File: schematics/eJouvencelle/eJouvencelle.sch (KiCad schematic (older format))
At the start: 28 parts

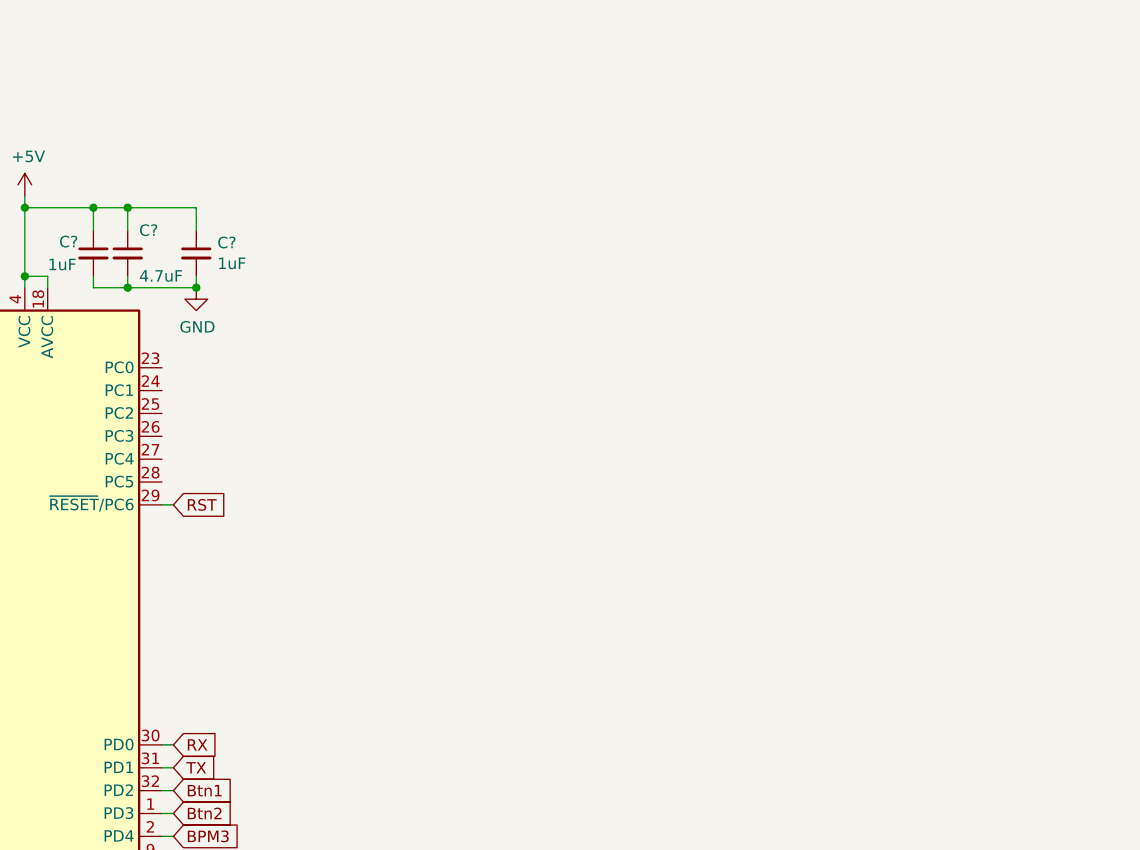
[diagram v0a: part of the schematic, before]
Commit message: add 7-segment w/ CD4511
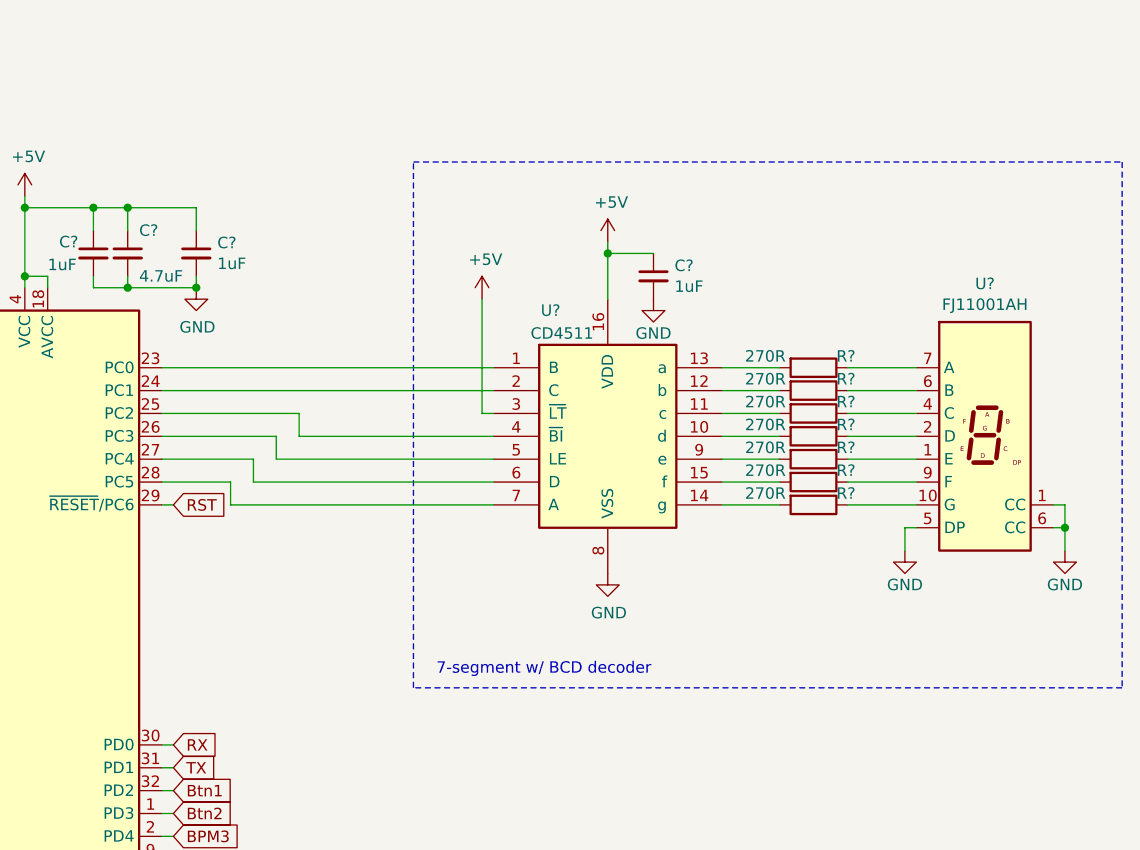
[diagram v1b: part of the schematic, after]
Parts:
- added C?: 1uF, symbol Device:C_Small
- added R? (x7): 270R, symbol Device:R
- added U?: CD4511, symbol eJouvencelle:CD4511
- added U?: FJ11001AH, Display_7Segment:HDSP-7801, symbol eJouvencelle:FJ11001AH
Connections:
- net +5V: now also C?.1, U?.16 (VDD), U?.3 (~LT)
- net GND: now also C?.2, U?.1 (E), U?.5 (DP), U?.6 (CC), U?.8 (VSS)
- net at U?.23 (PC0): now also U?.1 (B)
- net at U?.24 (PC1): now also U?.2 (C)
- net at U?.25 (PC2): now also U?.4 (~BI)
- net at U?.26 (PC3): now also U?.5 (LE)
- net at U?.27 (PC4): now also U?.6 (D)
- net at U?.28 (PC5): now also U?.7 (A)
- new net: R?.2, U?.10 (d)
- new net: R?.2, U?.11 (c)
- new net: R?.2, U?.12 (b)
- new net: R?.2, U?.13 (a)
- new net: R?.2, U?.14 (g)
- new net: R?.2, U?.15 (f)
- new net: R?.2, U?.9 (e)
- new net: R?.1, U?.7 (A)
- new net: R?.1, U?.6 (CC)
- new net: R?.1, U?.4 (C)
- new net: R?.1, U?.2 (D)
- new net: R?.1, U?.1 (E)
- new net: R?.1, U?.9 (F)
- new net: R?.1, U?.10 (G)
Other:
- note added: "7-segment w/ BCD decoder"

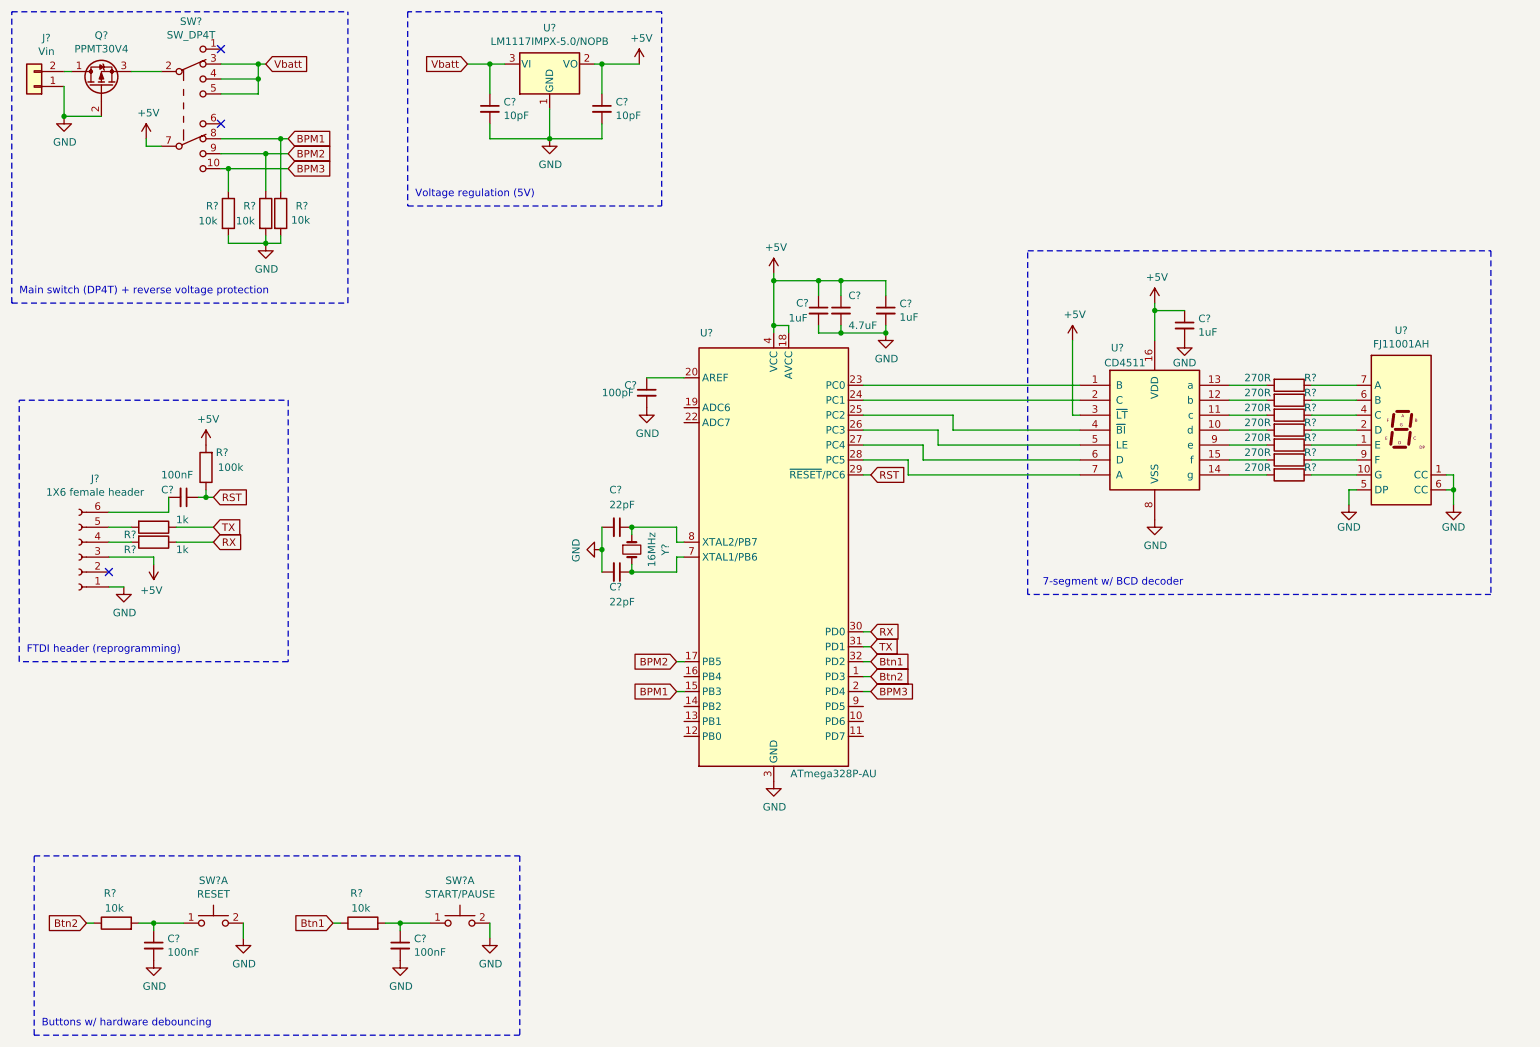
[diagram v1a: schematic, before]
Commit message: add MOSFET-driven buzzer
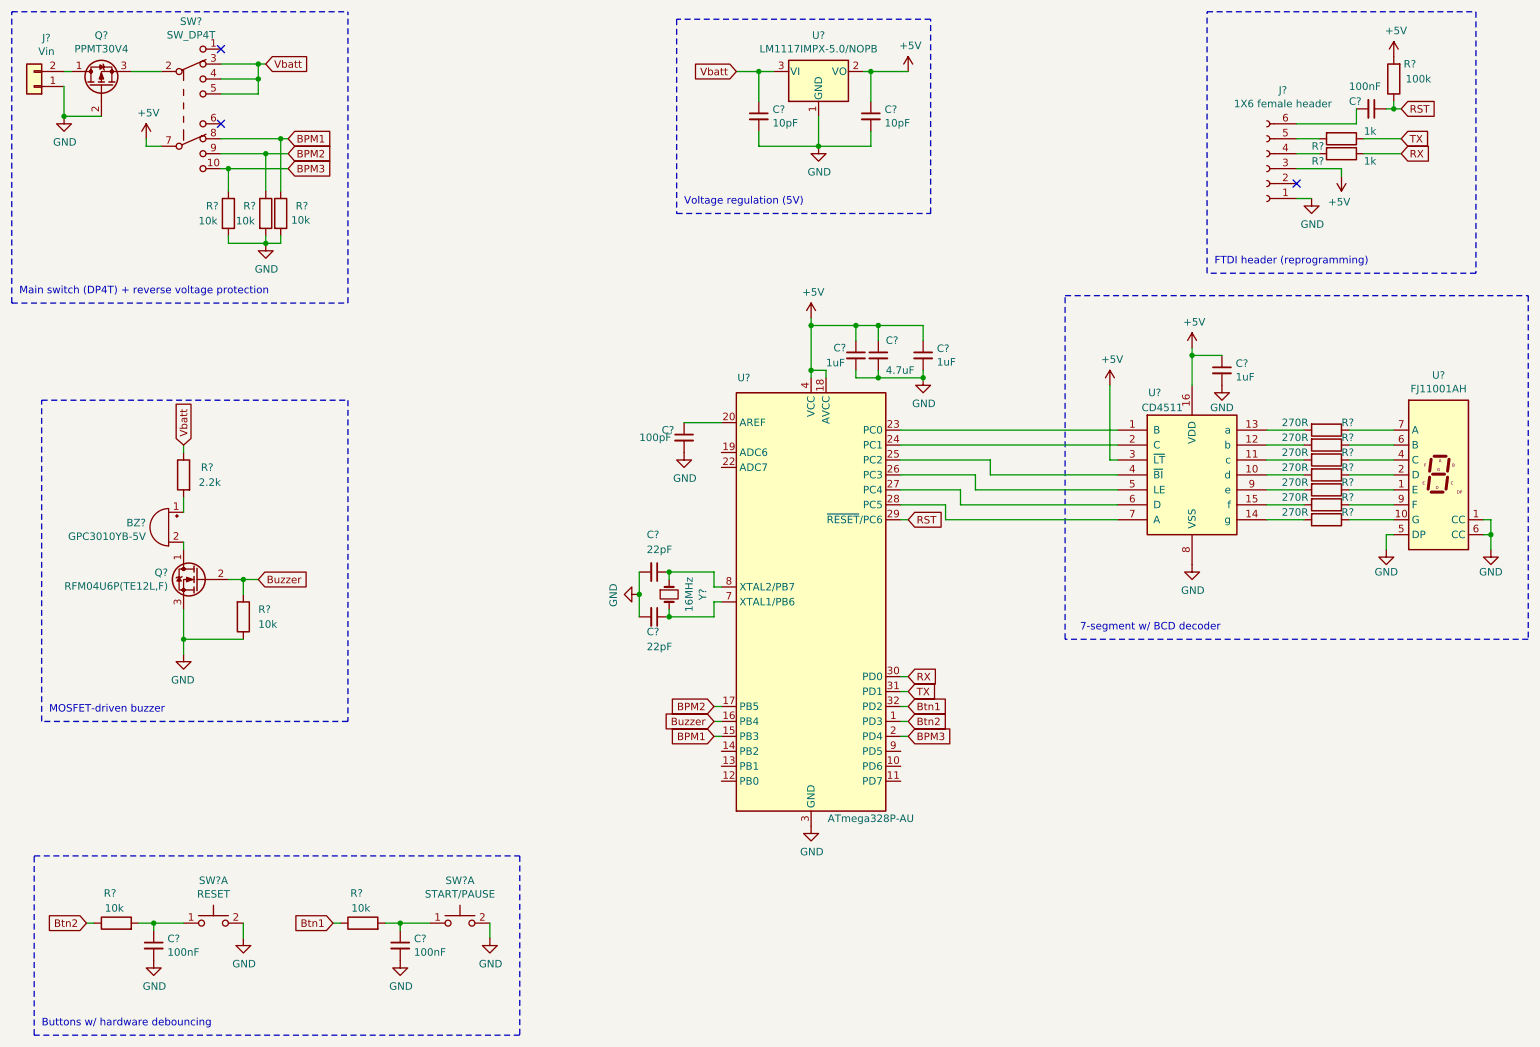
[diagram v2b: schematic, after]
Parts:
- added BZ?: GPC3010YB-5V, symbol Device:Buzzer
- added Q?: RFM04U6P(TE12L,F), symbol Device:Q_NMOS_DGS
- added R?: 2.2k, symbol Device:R
- added R?: 10k, symbol Device:R
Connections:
- net GND: now also Q?.3 (S), R?.1
- net Vbatt: now also R?.1
- net Buzzer: now reaches U?.16 (PB4)
- net Buzzer: now also Q?.2 (G), R?.2
- new net: BZ?.1 (-), R?.2
- new net: BZ?.2 (+), Q?.1 (D)
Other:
- note added: "MOSFET-driven buzzer"
- moved on the sheet: C?, J?, R?, U?, Y?
